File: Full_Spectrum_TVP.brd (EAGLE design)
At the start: 50.8 x 50.8 mm, 22 parts, among them Q2 BSS138, Q3 BSS138, U1 AP7312-3.3/1.8, X1 AS7421, X2 AS7343

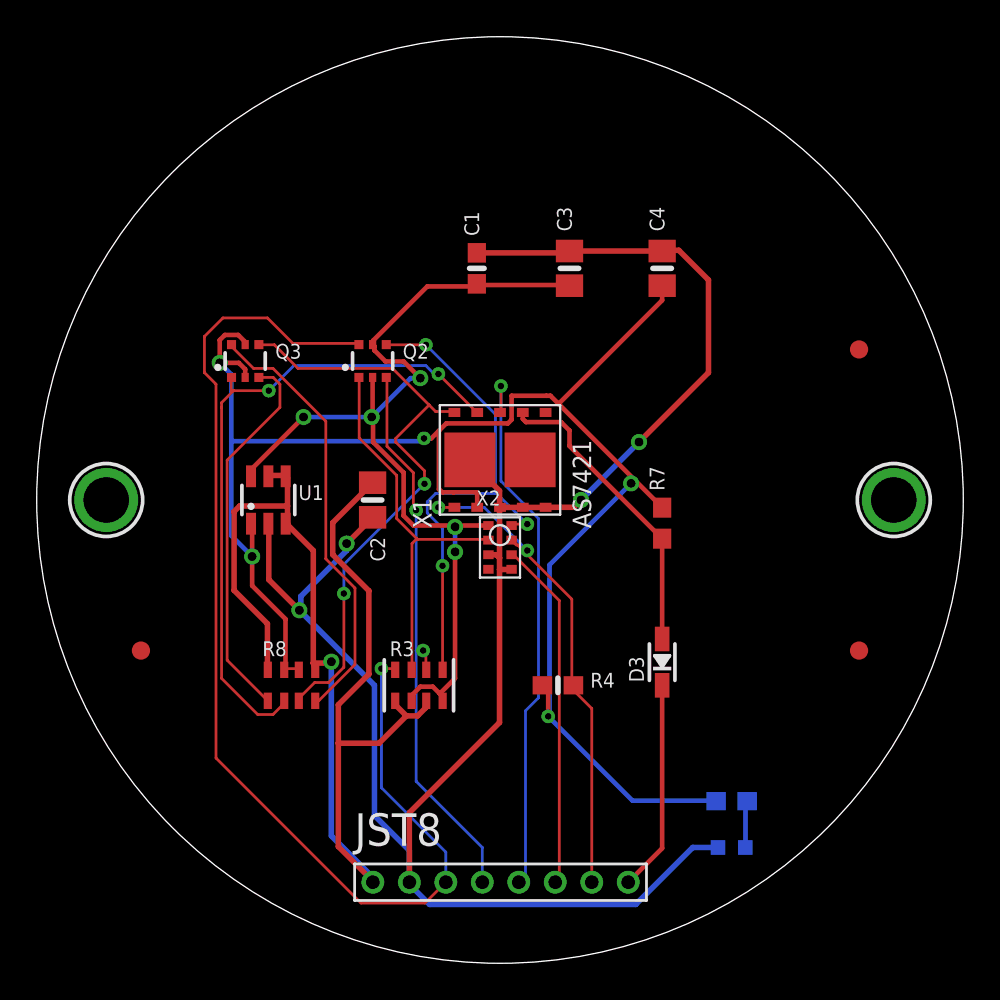
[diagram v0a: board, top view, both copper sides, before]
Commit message: Add files via upload
Revisions to the traces and spacing. No changes to the schematic.
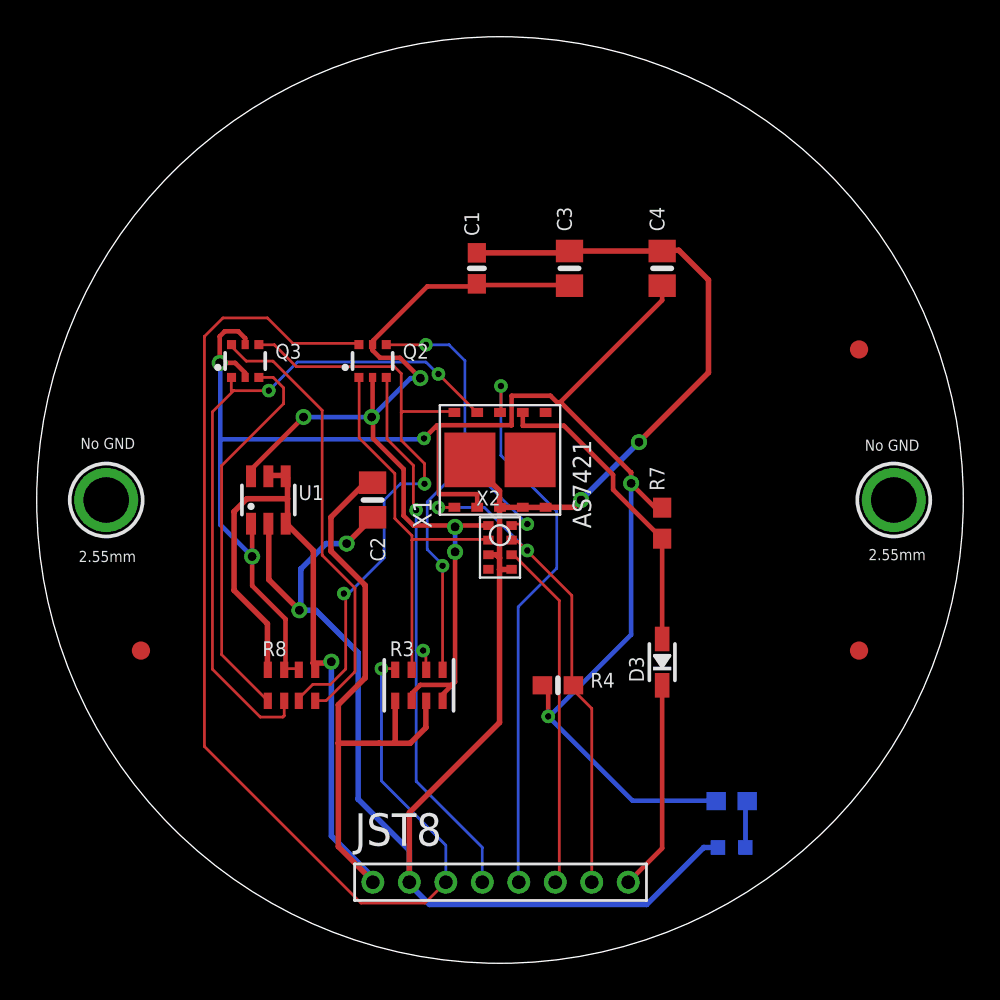
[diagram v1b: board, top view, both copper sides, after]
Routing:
- net VCC: track 71.1 -> 73.3 mm
- net 3.3V: track 97.0 -> 98.6 mm
- net GND: track 109.0 -> 110.2 mm
- net RX/SCL_3V: track 33.2 -> 34.3 mm
- net TX/SDA_3V: track 36.6 -> 37.6 mm
- net GPIO0: track 30.0 -> 30.8 mm
- net 1.8V: track 53.0 -> 53.6 mm
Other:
- board text added: "2.55mm"
- board text added: "No GND"
